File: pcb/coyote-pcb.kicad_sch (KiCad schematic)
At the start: 13 parts, among them U1 Basalt

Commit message: Lots of small updates
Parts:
- added H1, H2, H3, H4: MountingHole_Pad, MountingHole:MountingHole_3.2mm_M3_Pad, symbol Mechanical:MountingHole_Pad
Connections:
- net GND: now also H1.1, H2.1, H3.1, H4.1

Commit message: Add silkscreen logo etc, update title blocks
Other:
- company: (none) -> MESA
- title: (none) -> Coyote
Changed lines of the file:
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@@
 	(generator_version "10.0")
 	(paper "A4")
+	(title_block
+		(title "Coyote")
+		(date "2026-05-10")
+		(rev "1")
+		(company "MESA")
+	)
 	(junction
 		(at 124.46 152.4)

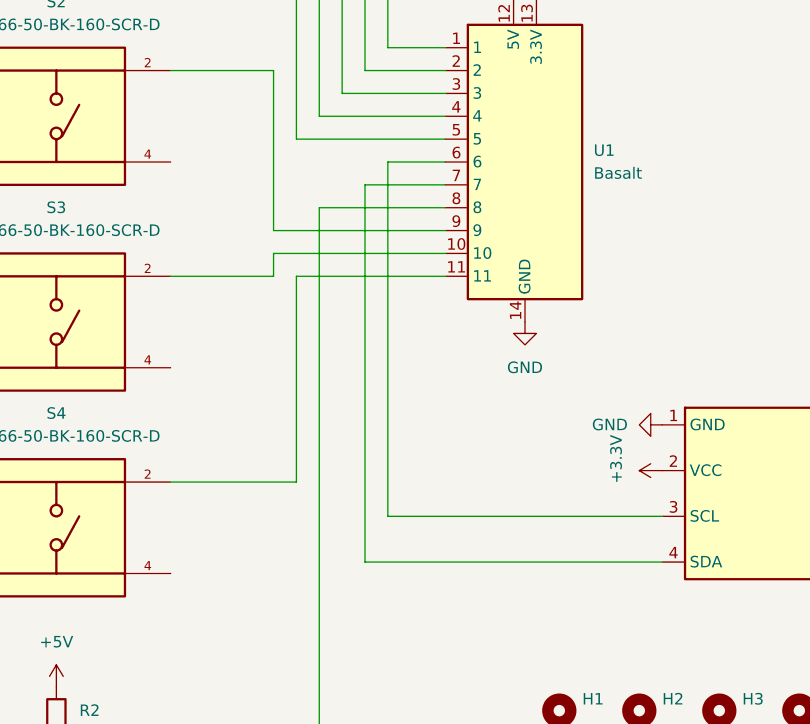
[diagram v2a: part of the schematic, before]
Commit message: Add dimensional drawing and STEP file
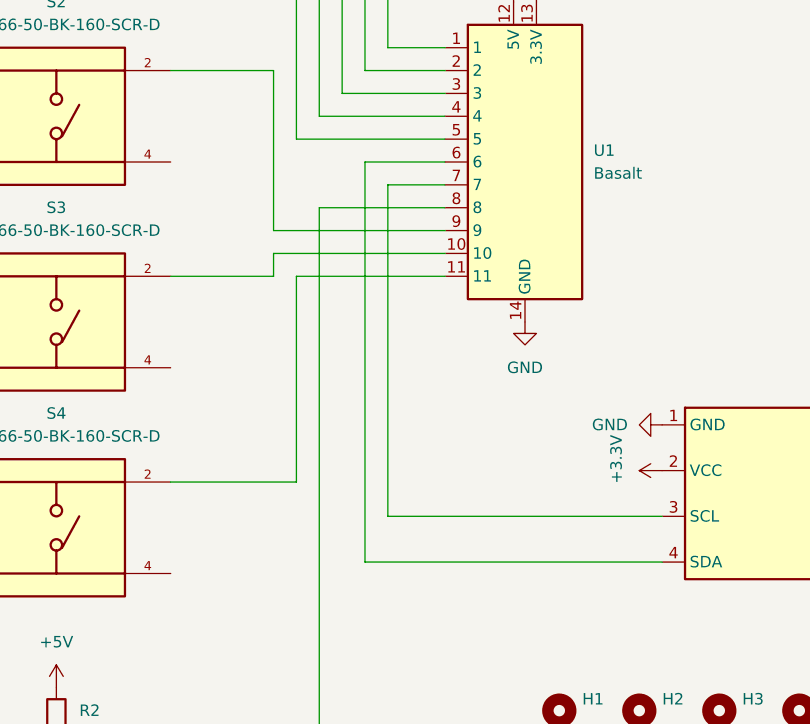
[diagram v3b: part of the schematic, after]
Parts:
- U1: footprint my-kicad-parts:MESA_Basalt -> my-kicad-parts:MESA_Basalt_RevA
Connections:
- net at U1.6: now also DS1.4 (SDA); no longer DS1.3 (SCL)
- net at U1.7: now also DS1.3 (SCL); no longer DS1.4 (SDA)
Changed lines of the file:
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@@
 	(title_block
 		(title "Coyote")
-		(date "2026-05-10")
-		(rev "1")
+		(date "2026-05-28")
+		(rev "A")
 		(company "MESA")
 	)
@@
 	(wire
 		(pts
-			(xy 161.29 86.36) (xy 161.29 125.73)
-		)
-		(stroke
-			(width 0)
-			(type default)
-		)
-	)
-	(wire
-		(pts
 			(xy 161.29 46.99) (xy 161.29 73.66)
 		)
@@
 	(wire
 		(pts
-			(xy 158.75 88.9) (xy 167.64 88.9)
+			(xy 161.29 88.9) (xy 167.64 88.9)
 		)
 		(stroke
@@
 	(wire
 		(pts
-			(xy 161.29 86.36) (xy 167.64 86.36)
-		)
-		(stroke
-			(width 0)
-			(type default)
-		)
-	)
-	(wire
-		(pts
 			(xy 148.59 93.98) (xy 167.64 93.98)
 		)
@@
 	(wire
 		(pts
+			(xy 158.75 86.36) (xy 158.75 130.81)
+		)
+		(stroke
+			(width 0)
+			(type default)
+		)
+	)
+	(wire
+		(pts
 			(xy 161.29 125.73) (xy 191.77 125.73)
 		)
@@
 	(wire
 		(pts
-			(xy 158.75 88.9) (xy 158.75 130.81)
+			(xy 161.29 88.9) (xy 161.29 125.73)
 		)
 		(stroke
@@
 		(pts
 			(xy 153.67 91.44) (xy 167.64 91.44)
+		)
+		(stroke
+			(width 0)
+			(type default)
+		)
+	)
+	(wire
+		(pts
+			(xy 167.64 86.36) (xy 158.75 86.36)
 		)
 		(stroke
@@
 			)
 		)
-		(property "Footprint" "my-kicad-parts:MESA_Basalt"
+		(property "Footprint" "my-kicad-parts:MESA_Basalt_RevA"
 			(at 176.53 86.36 0)
 			(hide yes)
